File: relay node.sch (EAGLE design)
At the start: 25 parts, among them J1 Channels, J2 LED, J3 PROG, J4 AUX, U1 ESP-WROOM-02U, U2 MCP23018-E/SS, U3 TLV75533

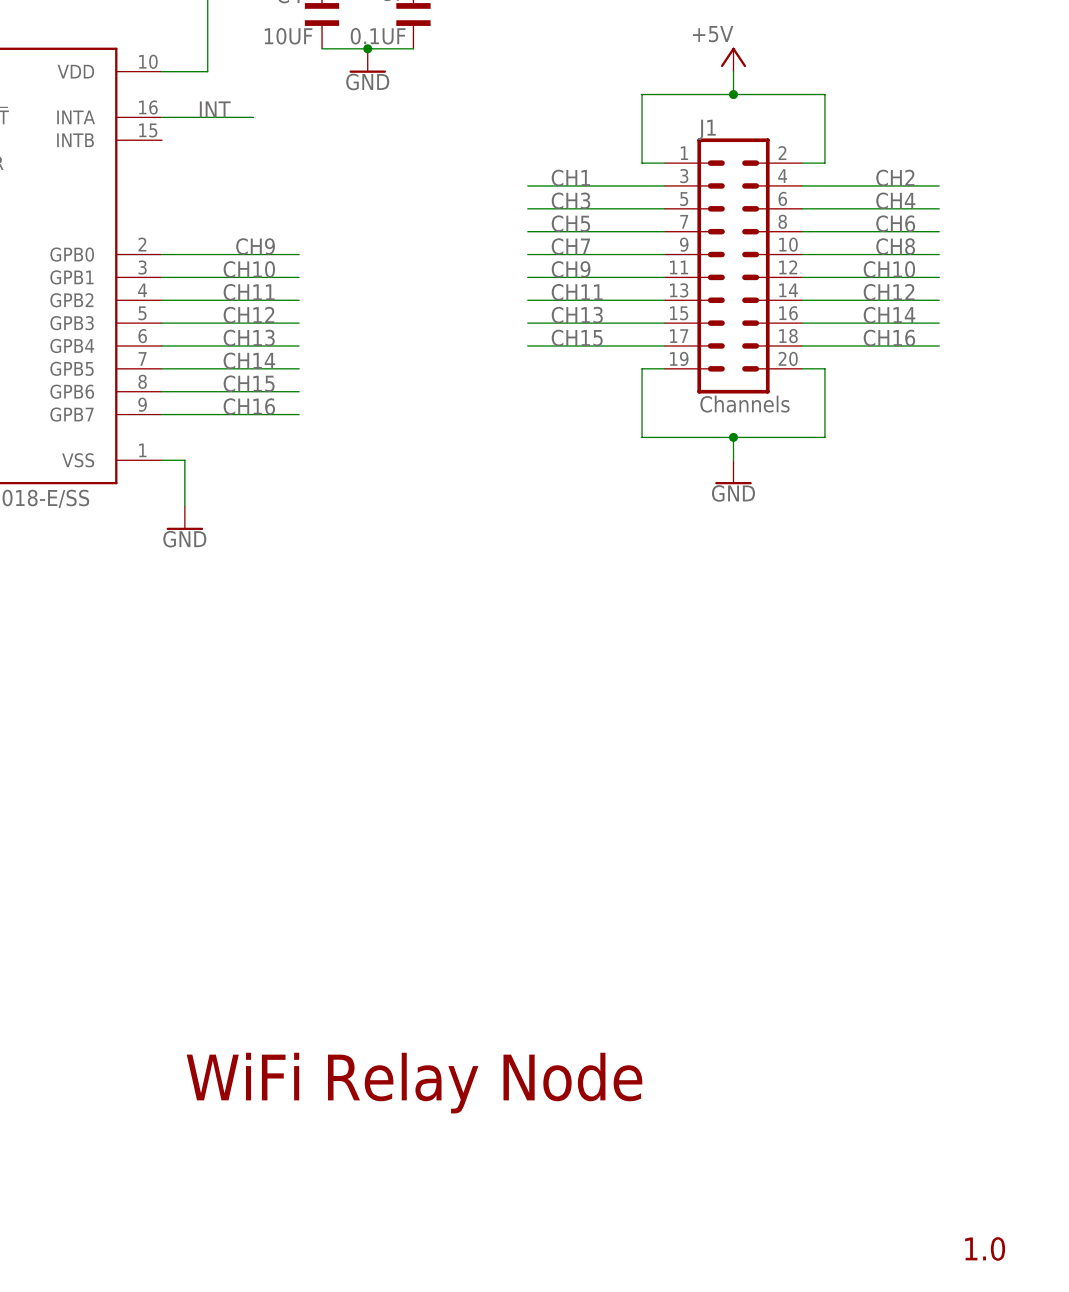
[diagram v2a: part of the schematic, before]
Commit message: Move J1 to bottom layer Add J1 to J3 connectors to BOM for quotes
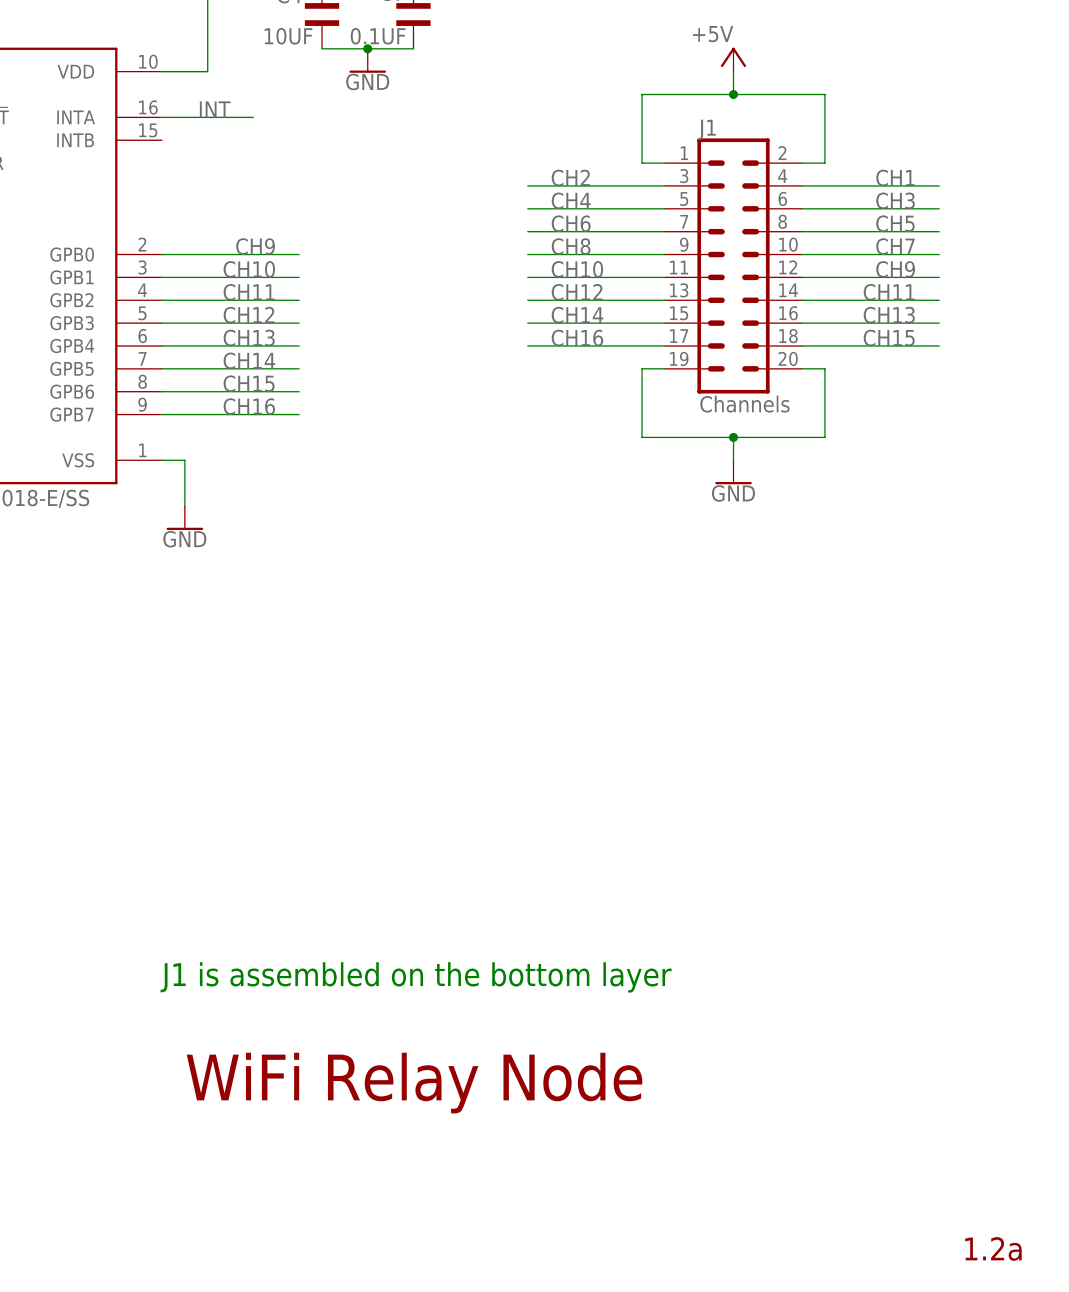
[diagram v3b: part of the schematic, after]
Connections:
- net CH1: now also J1.4; no longer J1.3
- net CH10: now also J1.11; no longer J1.12
- net CH11: now also J1.14; no longer J1.13
- net CH12: now also J1.13; no longer J1.14
- net CH13: now also J1.16; no longer J1.15
- net CH14: now also J1.15; no longer J1.16
- net CH15: now also J1.18; no longer J1.17
- net CH16: now also J1.17; no longer J1.18
- net CH2: now also J1.3; no longer J1.4
- net CH3: now also J1.6; no longer J1.5
- net CH4: now also J1.5; no longer J1.6
- net CH5: now also J1.8; no longer J1.7
- net CH6: now also J1.7; no longer J1.8
- net CH7: now also J1.10; no longer J1.9
- net CH8: now also J1.9; no longer J1.10
- net CH9: now also J1.12; no longer J1.11
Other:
- note added: "1.2a"
- note added: "J1 is assembled on the bottom layer"
- note removed: "1.0"
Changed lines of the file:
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@@
 <sheet>
 <plain>
-<text x="264.16" y="7.62" size="2.54" layer="94" font="vector" ratio="7" distance="3">1.0</text>
+<text x="264.16" y="7.62" size="2.54" layer="94" font="vector" ratio="7" distance="3">1.2a</text>
 <text x="177.8" y="25.4" size="5.08" layer="94" font="vector" ratio="7" distance="3">WiFi Relay Node</text>
+<text x="175.26" y="38.1" size="2.54" layer="91">J1 is assembled on the bottom layer</text>
 </plain>
 <instances>
@@
 </segment>
 <segment>
+<pinref part="J1" gate="G$1" pin="4"/>
+<wire x1="246.38" y1="127" x2="261.62" y2="127" width="0.1524" layer="91"/>
+<label x="259.08" y="127" size="1.778" layer="95" align="bottom-right"/>
+</segment>
+</net>
+<net name="CH2" class="0">
+<segment>
+<pinref part="U2" gate="G$1" pin="GPA1"/>
+<wire x1="144.78" y1="116.84" x2="129.54" y2="116.84" width="0.1524" layer="91"/>
+<label x="132.08" y="116.84" size="1.778" layer="95"/>
+</segment>
+<segment>
 <pinref part="J1" gate="G$1" pin="3"/>
 <wire x1="231.14" y1="127" x2="215.9" y2="127" width="0.1524" layer="91"/>
@@
 </segment>
 </net>
-<net name="CH2" class="0">
-<segment>
-<pinref part="U2" gate="G$1" pin="GPA1"/>
-<wire x1="144.78" y1="116.84" x2="129.54" y2="116.84" width="0.1524" layer="91"/>
-<label x="132.08" y="116.84" size="1.778" layer="95"/>
-</segment>
-<segment>
-<pinref part="J1" gate="G$1" pin="4"/>
-<wire x1="246.38" y1="127" x2="261.62" y2="127" width="0.1524" layer="91"/>
-<label x="259.08" y="127" size="1.778" layer="95" align="bottom-right"/>
-</segment>
-</net>
 <net name="CH3" class="0">
 <segment>
@@
 </segment>
 <segment>
+<pinref part="J1" gate="G$1" pin="6"/>
+<wire x1="246.38" y1="124.46" x2="261.62" y2="124.46" width="0.1524" layer="91"/>
+<label x="259.08" y="124.46" size="1.778" layer="95" align="bottom-right"/>
+</segment>
+</net>
+<net name="CH4" class="0">
+<segment>
+<pinref part="U2" gate="G$1" pin="GPA3"/>
+<wire x1="144.78" y1="111.76" x2="129.54" y2="111.76" width="0.1524" layer="91"/>
+<label x="132.08" y="111.76" size="1.778" layer="95"/>
+</segment>
+<segment>
 <pinref part="J1" gate="G$1" pin="5"/>
 <wire x1="231.14" y1="124.46" x2="215.9" y2="124.46" width="0.1524" layer="91"/>
@@
 </segment>
 </net>
-<net name="CH4" class="0">
-<segment>
-<pinref part="U2" gate="G$1" pin="GPA3"/>
-<wire x1="144.78" y1="111.76" x2="129.54" y2="111.76" width="0.1524" layer="91"/>
-<label x="132.08" y="111.76" size="1.778" layer="95"/>
-</segment>
-<segment>
-<pinref part="J1" gate="G$1" pin="6"/>
-<wire x1="246.38" y1="124.46" x2="261.62" y2="124.46" width="0.1524" layer="91"/>
-<label x="259.08" y="124.46" size="1.778" layer="95" align="bottom-right"/>
-</segment>
-</net>
 <net name="CH5" class="0">
 <segment>
@@
 </segment>
 <segment>
+<pinref part="J1" gate="G$1" pin="8"/>
+<wire x1="246.38" y1="121.92" x2="261.62" y2="121.92" width="0.1524" layer="91"/>
+<label x="259.08" y="121.92" size="1.778" layer="95" align="bottom-right"/>
+</segment>
+</net>
+<net name="CH6" class="0">
+<segment>
+<pinref part="U2" gate="G$1" pin="GPA5"/>
+<wire x1="144.78" y1="106.68" x2="129.54" y2="106.68" width="0.1524" layer="91"/>
+<label x="132.08" y="106.68" size="1.778" layer="95"/>
+</segment>
+<segment>
 <pinref part="J1" gate="G$1" pin="7"/>
 <wire x1="231.14" y1="121.92" x2="215.9" y2="121.92" width="0.1524" layer="91"/>
@@
 </segment>
 </net>
-<net name="CH6" class="0">
-<segment>
-<pinref part="U2" gate="G$1" pin="GPA5"/>
-<wire x1="144.78" y1="106.68" x2="129.54" y2="106.68" width="0.1524" layer="91"/>
-<label x="132.08" y="106.68" size="1.778" layer="95"/>
-</segment>
-<segment>
-<pinref part="J1" gate="G$1" pin="8"/>
-<wire x1="246.38" y1="121.92" x2="261.62" y2="121.92" width="0.1524" layer="91"/>
-<label x="259.08" y="121.92" size="1.778" layer="95" align="bottom-right"/>
-</segment>
-</net>
 <net name="CH7" class="0">
 <segment>
@@
 </segment>
 <segment>
+<pinref part="J1" gate="G$1" pin="10"/>
+<wire x1="246.38" y1="119.38" x2="261.62" y2="119.38" width="0.1524" layer="91"/>
+<label x="259.08" y="119.38" size="1.778" layer="95" align="bottom-right"/>
+</segment>
+</net>
+<net name="CH8" class="0">
+<segment>
+<pinref part="U2" gate="G$1" pin="GPA7"/>
+<wire x1="144.78" y1="101.6" x2="129.54" y2="101.6" width="0.1524" layer="91"/>
+<label x="132.08" y="101.6" size="1.778" layer="95"/>
+</segment>
+<segment>
 <pinref part="J1" gate="G$1" pin="9"/>
 <wire x1="231.14" y1="119.38" x2="215.9" y2="119.38" width="0.1524" layer="91"/>
@@
 </segment>
 </net>
-<net name="CH8" class="0">
-<segment>
-<pinref part="U2" gate="G$1" pin="GPA7"/>
-<wire x1="144.78" y1="101.6" x2="129.54" y2="101.6" width="0.1524" layer="91"/>
-<label x="132.08" y="101.6" size="1.778" layer="95"/>
-</segment>
-<segment>
-<pinref part="J1" gate="G$1" pin="10"/>
-<wire x1="246.38" y1="119.38" x2="261.62" y2="119.38" width="0.1524" layer="91"/>
-<label x="259.08" y="119.38" size="1.778" layer="95" align="bottom-right"/>
-</segment>
-</net>
 <net name="CH9" class="0">
 <segment>
@@
 </segment>
 <segment>
+<pinref part="J1" gate="G$1" pin="12"/>
+<wire x1="246.38" y1="116.84" x2="261.62" y2="116.84" width="0.1524" layer="91"/>
+<label x="259.08" y="116.84" size="1.778" layer="95" align="bottom-right"/>
+</segment>
+</net>
+<net name="CH10" class="0">
+<segment>
+<pinref part="U2" gate="G$1" pin="GPB1"/>
+<wire x1="175.26" y1="116.84" x2="190.5" y2="116.84" width="0.1524" layer="91"/>
+<label x="187.96" y="116.84" size="1.778" layer="95" align="bottom-right"/>
+</segment>
+<segment>
 <pinref part="J1" gate="G$1" pin="11"/>
 <wire x1="231.14" y1="116.84" x2="215.9" y2="116.84" width="0.1524" layer="91"/>
@@
 </segment>
 </net>
-<net name="CH10" class="0">
-<segment>
-<pinref part="U2" gate="G$1" pin="GPB1"/>
-<wire x1="175.26" y1="116.84" x2="190.5" y2="116.84" width="0.1524" layer="91"/>
-<label x="187.96" y="116.84" size="1.778" layer="95" align="bottom-right"/>
-</segment>
-<segment>
-<pinref part="J1" gate="G$1" pin="12"/>
-<wire x1="246.38" y1="116.84" x2="261.62" y2="116.84" width="0.1524" layer="91"/>
-<label x="259.08" y="116.84" size="1.778" layer="95" align="bottom-right"/>
-</segment>
-</net>
 <net name="CH11" class="0">
 <segment>
@@
 </segment>
 <segment>
+<pinref part="J1" gate="G$1" pin="14"/>
+<wire x1="246.38" y1="114.3" x2="261.62" y2="114.3" width="0.1524" layer="91"/>
+<label x="259.08" y="114.3" size="1.778" layer="95" align="bottom-right"/>
+</segment>
+</net>
+<net name="CH12" class="0">
+<segment>
+<pinref part="U2" gate="G$1" pin="GPB3"/>
+<wire x1="175.26" y1="111.76" x2="190.5" y2="111.76" width="0.1524" layer="91"/>
+<label x="187.96" y="111.76" size="1.778" layer="95" align="bottom-right"/>
+</segment>
+<segment>
 <pinref part="J1" gate="G$1" pin="13"/>
 <wire x1="231.14" y1="114.3" x2="215.9" y2="114.3" width="0.1524" layer="91"/>
@@
 </segment>
 </net>
-<net name="CH12" class="0">
-<segment>
-<pinref part="U2" gate="G$1" pin="GPB3"/>
-<wire x1="175.26" y1="111.76" x2="190.5" y2="111.76" width="0.1524" layer="91"/>
-<label x="187.96" y="111.76" size="1.778" layer="95" align="bottom-right"/>
-</segment>
-<segment>
-<pinref part="J1" gate="G$1" pin="14"/>
-<wire x1="246.38" y1="114.3" x2="261.62" y2="114.3" width="0.1524" layer="91"/>
-<label x="259.08" y="114.3" size="1.778" layer="95" align="bottom-right"/>
-</segment>
-</net>
 <net name="CH13" class="0">
 <segment>
@@
 </segment>
 <segment>
+<pinref part="J1" gate="G$1" pin="16"/>
+<wire x1="246.38" y1="111.76" x2="261.62" y2="111.76" width="0.1524" layer="91"/>
+<label x="259.08" y="111.76" size="1.778" layer="95" align="bottom-right"/>
+</segment>
+</net>
+<net name="CH14" class="0">
+<segment>
+<pinref part="U2" gate="G$1" pin="GPB5"/>
+<wire x1="175.26" y1="106.68" x2="190.5" y2="106.68" width="0.1524" layer="91"/>
+<label x="187.96" y="106.68" size="1.778" layer="95" align="bottom-right"/>
+</segment>
+<segment>
 <pinref part="J1" gate="G$1" pin="15"/>
 <wire x1="231.14" y1="111.76" x2="215.9" y2="111.76" width="0.1524" layer="91"/>
@@
 </segment>
 </net>
-<net name="CH14" class="0">
-<segment>
-<pinref part="U2" gate="G$1" pin="GPB5"/>
-<wire x1="175.26" y1="106.68" x2="190.5" y2="106.68" width="0.1524" layer="91"/>
-<label x="187.96" y="106.68" size="1.778" layer="95" align="bottom-right"/>
-</segment>
-<segment>
-<pinref part="J1" gate="G$1" pin="16"/>
-<wire x1="246.38" y1="111.76" x2="261.62" y2="111.76" width="0.1524" layer="91"/>
-<label x="259.08" y="111.76" size="1.778" layer="95" align="bottom-right"/>
-</segment>
-</net>
 <net name="CH15" class="0">
 <segment>
@@
 </segment>
 <segment>
+<pinref part="J1" gate="G$1" pin="18"/>
+<wire x1="246.38" y1="109.22" x2="261.62" y2="109.22" width="0.1524" layer="91"/>
+<label x="259.08" y="109.22" size="1.778" layer="95" align="bottom-right"/>
+</segment>
+</net>
+<net name="CH16" class="0">
+<segment>
+<pinref part="U2" gate="G$1" pin="GPB7"/>
+<wire x1="175.26" y1="101.6" x2="190.5" y2="101.6" width="0.1524" layer="91"/>
+<label x="187.96" y="101.6" size="1.778" layer="95" align="bottom-right"/>
+</segment>
+<segment>
 <pinref part="J1" gate="G$1" pin="17"/>
 <wire x1="231.14" y1="109.22" x2="215.9" y2="109.22" width="0.1524" layer="91"/>
@@
 </segment>
 </net>
-<net name="CH16" class="0">
-<segment>
-<pinref part="U2" gate="G$1" pin="GPB7"/>
-<wire x1="175.26" y1="101.6" x2="190.5" y2="101.6" width="0.1524" layer="91"/>
-<label x="187.96" y="101.6" size="1.778" layer="95" align="bottom-right"/>
-</segment>
-<segment>
-<pinref part="J1" gate="G$1" pin="18"/>
-<wire x1="246.38" y1="109.22" x2="261.62" y2="109.22" width="0.1524" layer="91"/>
-<label x="259.08" y="109.22" size="1.778" layer="95" align="bottom-right"/>
-</segment>
-</net>
